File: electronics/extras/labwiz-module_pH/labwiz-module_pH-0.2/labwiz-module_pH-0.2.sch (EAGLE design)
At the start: 14 parts, among them U3 XC6206P182MR, U4 OPA333DBV

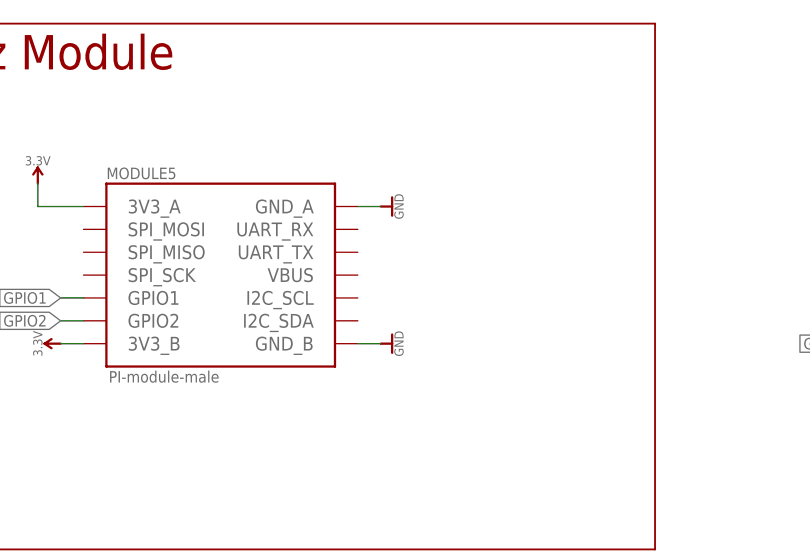
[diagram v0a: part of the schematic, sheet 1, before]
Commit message: Fixed VBUS issues on pH module.
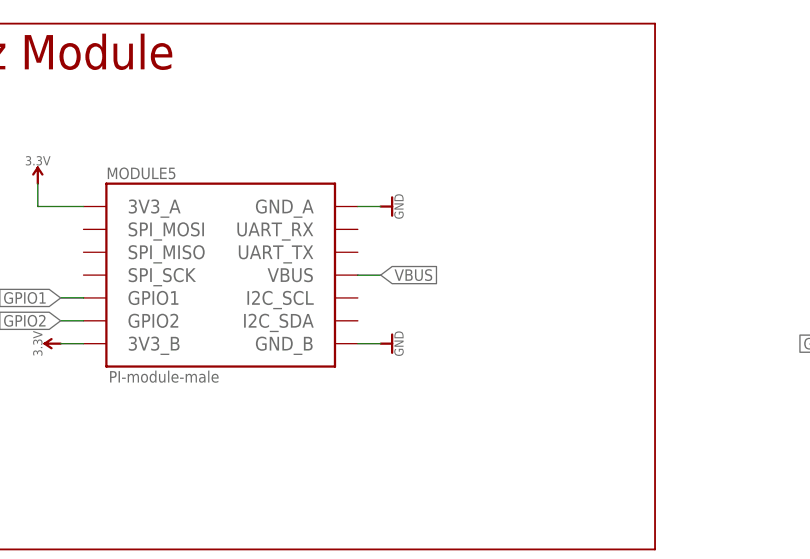
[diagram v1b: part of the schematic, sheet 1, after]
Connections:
- net VBUS: now also MODULE5.VBUS
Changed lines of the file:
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@@
 <grid distance="0.1" unitdist="inch" unit="inch" style="lines" multiple="1" display="no" altdistance="0.01" altunitdist="inch" altunit="inch"/>
 <layers>
-<layer number="1" name="Top" color="4" fill="1" visible="yes" active="no"/>
-<layer number="2" name="Route2" color="1" fill="3" visible="yes" active="no"/>
-<layer number="3" name="Route3" color="4" fill="3" visible="yes" active="no"/>
-<layer number="4" name="Route4" color="1" fill="4" visible="yes" active="no"/>
-<layer number="5" name="Route5" color="4" fill="4" visible="yes" active="no"/>
-<layer number="6" name="Route6" color="1" fill="8" visible="yes" active="no"/>
-<layer number="7" name="Route7" color="4" fill="8" visible="yes" active="no"/>
-<layer number="8" name="Route8" color="1" fill="2" visible="yes" active="no"/>
-<layer number="9" name="Route9" color="4" fill="2" visible="yes" active="no"/>
-<layer number="10" name="Route10" color="1" fill="7" visible="yes" active="no"/>
-<layer number="11" name="Route11" color="4" fill="7" visible="yes" active="no"/>
-<layer number="12" name="Route12" color="1" fill="5" visible="yes" active="no"/>
-<layer number="13" name="Route13" color="4" fill="5" visible="yes" active="no"/>
-<layer number="14" name="Route14" color="1" fill="6" visible="yes" active="no"/>
-<layer number="15" name="Route15" color="4" fill="6" visible="yes" active="no"/>
-<layer number="16" name="Bottom" color="1" fill="1" visible="yes" active="no"/>
-<layer number="17" name="Pads" color="2" fill="1" visible="yes" active="no"/>
-<layer number="18" name="Vias" color="2" fill="1" visible="yes" active="no"/>
-<layer number="19" name="Unrouted" color="6" fill="1" visible="yes" active="no"/>
-<layer number="20" name="Dimension" color="13" fill="1" visible="yes" active="no"/>
-<layer number="21" name="tPlace" color="7" fill="1" visible="yes" active="no"/>
-<layer number="22" name="bPlace" color="14" fill="1" visible="yes" active="no"/>
-<layer number="23" name="tOrigins" color="15" fill="1" visible="yes" active="no"/>
-<layer number="24" name="bOrigins" color="15" fill="1" visible="yes" active="no"/>
-<layer number="25" name="tNames" color="7" fill="1" visible="yes" active="no"/>
-<layer number="26" name="bNames" color="7" fill="1" visible="yes" active="no"/>
-<layer number="27" name="tValues" color="7" fill="1" visible="yes" active="no"/>
-<layer number="28" name="bValues" color="7" fill="1" visible="yes" active="no"/>
+<layer number="1" name="Top" color="4" fill="1" visible="no" active="no"/>
+<layer number="2" name="Route2" color="1" fill="3" visible="no" active="no"/>
+<layer number="3" name="Route3" color="4" fill="3" visible="no" active="no"/>
+<layer number="4" name="Route4" color="1" fill="4" visible="no" active="no"/>
+<layer number="5" name="Route5" color="4" fill="4" visible="no" active="no"/>
+<layer number="6" name="Route6" color="1" fill="8" visible="no" active="no"/>
+<layer number="7" name="Route7" color="4" fill="8" visible="no" active="no"/>
+<layer number="8" name="Route8" color="1" fill="2" visible="no" active="no"/>
+<layer number="9" name="Route9" color="4" fill="2" visible="no" active="no"/>
+<layer number="10" name="Route10" color="1" fill="7" visible="no" active="no"/>
+<layer number="11" name="Route11" color="4" fill="7" visible="no" active="no"/>
+<layer number="12" name="Route12" color="1" fill="5" visible="no" active="no"/>
+<layer number="13" name="Route13" color="4" fill="5" visible="no" active="no"/>
+<layer number="14" name="Route14" color="1" fill="6" visible="no" active="no"/>
+<layer number="15" name="Route15" color="4" fill="6" visible="no" active="no"/>
+<layer number="16" name="Bottom" color="1" fill="1" visible="no" active="no"/>
+<layer number="17" name="Pads" color="2" fill="1" visible="no" active="no"/>
+<layer number="18" name="Vias" color="2" fill="1" visible="no" active="no"/>
+<layer number="19" name="Unrouted" color="6" fill="1" visible="no" active="no"/>
+<layer number="20" name="Dimension" color="13" fill="1" visible="no" active="no"/>
+<layer number="21" name="tPlace" color="7" fill="1" visible="no" active="no"/>
+<layer number="22" name="bPlace" color="14" fill="1" visible="no" active="no"/>
+<layer number="23" name="tOrigins" color="15" fill="1" visible="no" active="no"/>
+<layer number="24" name="bOrigins" color="15" fill="1" visible="no" active="no"/>
+<layer number="25" name="tNames" color="7" fill="1" visible="no" active="no"/>
+<layer number="26" name="bNames" color="7" fill="1" visible="no" active="no"/>
+<layer number="27" name="tValues" color="7" fill="1" visible="no" active="no"/>
+<layer number="28" name="bValues" color="7" fill="1" visible="no" active="no"/>
 <layer number="29" name="tStop" color="7" fill="3" visible="no" active="no"/>
 <layer number="30" name="bStop" color="7" fill="6" visible="no" active="no"/>
@@
 <layer number="35" name="tGlue" color="7" fill="4" visible="no" active="no"/>
 <layer number="36" name="bGlue" color="7" fill="5" visible="no" active="no"/>
-<layer number="37" name="tTest" color="7" fill="1" visible="yes" active="no"/>
-<layer number="38" name="bTest" color="7" fill="1" visible="yes" active="no"/>
+<layer number="37" name="tTest" color="7" fill="1" visible="no" active="no"/>
+<layer number="38" name="bTest" color="7" fill="1" visible="no" active="no"/>
 <layer number="39" name="tKeepout" color="4" fill="11" visible="no" active="no"/>
 <layer number="40" name="bKeepout" color="1" fill="11" visible="no" active="no"/>
@@
 <layer number="44" name="Drills" color="7" fill="1" visible="no" active="no"/>
 <layer number="45" name="Holes" color="7" fill="1" visible="no" active="no"/>
-<layer number="46" name="Milling" color="3" fill="1" visible="yes" active="no"/>
-<layer number="47" name="Measures" color="7" fill="1" visible="yes" active="no"/>
-<layer number="48" name="Document" color="7" fill="1" visible="yes" active="no"/>
-<layer number="49" name="Reference" color="7" fill="1" visible="yes" active="no"/>
-<layer number="50" name="dxf" color="7" fill="1" visible="yes" active="no"/>
-<layer number="51" name="tDocu" color="6" fill="1" visible="yes" active="no"/>
-<layer number="52" name="bDocu" color="7" fill="1" visible="yes" active="no"/>
-<layer number="53" name="tGND_GNDA" color="7" fill="9" visible="yes" active="no"/>
-<layer number="54" name="bGND_GNDA" color="1" fill="9" visible="yes" active="no"/>
-<layer number="56" name="wert" color="7" fill="1" visible="yes" active="no"/>
-<layer number="57" name="tCAD" color="7" fill="1" visible="yes" active="no"/>
-<layer number="59" name="tCarbon" color="7" fill="1" visible="yes" active="no"/>
-<layer number="60" name="bCarbon" color="7" fill="1" visible="yes" active="no"/>
+<layer number="46" name="Milling" color="3" fill="1" visible="no" active="no"/>
+<layer number="47" name="Measures" color="7" fill="1" visible="no" active="no"/>
+<layer number="48" name="Document" color="7" fill="1" visible="no" active="no"/>
+<layer number="49" name="Reference" color="7" fill="1" visible="no" active="no"/>
+<layer number="50" name="dxf" color="7" fill="1" visible="no" active="no"/>
+<layer number="51" name="tDocu" color="6" fill="1" visible="no" active="no"/>
+<layer number="52" name="bDocu" color="7" fill="1" visible="no" active="no"/>
+<layer number="53" name="tGND_GNDA" color="7" fill="9" visible="no" active="no"/>
+<layer number="54" name="bGND_GNDA" color="1" fill="9" visible="no" active="no"/>
+<layer number="56" name="wert" color="7" fill="1" visible="no" active="no"/>
+<layer number="57" name="tCAD" color="7" fill="1" visible="no" active="no"/>
+<layer number="59" name="tCarbon" color="7" fill="1" visible="no" active="no"/>
+<layer number="60" name="bCarbon" color="7" fill="1" visible="no" active="no"/>
 <layer number="90" name="Modules" color="5" fill="1" visible="yes" active="yes"/>
 <layer number="91" name="Nets" color="2" fill="1" visible="yes" active="yes"/>
@@
 <label x="30.48" y="165.1" size="1.27" layer="95" rot="R180" xref="yes"/>
 </segment>
-</net>
+<segment>
+<pinref part="MODULE5" gate="G$1" pin="VBUS"/>
+<wire x1="63.5" y1="226.06" x2="66.04" y2="226.06" width="0.1524" layer="91"/>
+<label x="66.04" y="226.06" size="1.27" layer="95" xref="yes"/>
+</segment>
+</net>

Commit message: Small changes. Not sure what.
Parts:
- C3, C4: value CAPACITOR_FIXED_0603 -> 51pF
- R1, R2: value RESISTOR_FIXED_0603 -> 510k
- R4: value RESISTOR_FIXED_0603 -> 51k
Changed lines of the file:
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@@
 <part name="C8" library="PaxInstruments-RCL" deviceset="CAPACITOR_FIXED" device="_0603" technology="_100NF" value="100nF"/>
 <part name="U3" library="IC" deviceset="XC6206" device="MR" value="XC6206P182MR"/>
-<part name="R1" library="PaxInstruments-RCL" deviceset="RESISTOR_FIXED" device="_0603" value=""/>
+<part name="R1" library="PaxInstruments-RCL" deviceset="RESISTOR_FIXED" device="_0603" value="510k"/>
 <part name="U4" library="IC" deviceset="OPA333" device="DBV"/>
 <part name="C1" library="PaxInstruments-RCL" deviceset="CAPACITOR_FIXED" device="_0603" technology="_100NF" value="100nF"/>
 <part name="GND3" library="PaxInstruments-Aesthetics" deviceset="GND" device="" value="GND"/>
 <part name="GND4" library="PaxInstruments-Aesthetics" deviceset="GND" device="" value="GND"/>
-<part name="R2" library="PaxInstruments-RCL" deviceset="RESISTOR_FIXED" device="_0603" value=""/>
+<part name="R2" library="PaxInstruments-RCL" deviceset="RESISTOR_FIXED" device="_0603" value="510k"/>
 <part name="SUPPLY3" library="PaxInstruments-Aesthetics" deviceset="SYM_VCC" device="" technology="3.3V" value="3.3V"/>
-<part name="C3" library="PaxInstruments-RCL" deviceset="CAPACITOR_FIXED" device="_0603" value=""/>
+<part name="C3" library="PaxInstruments-RCL" deviceset="CAPACITOR_FIXED" device="_0603" value="51pF"/>
 <part name="GND5" library="PaxInstruments-Aesthetics" deviceset="GND" device="" value="GND"/>
-<part name="R4" library="PaxInstruments-RCL" deviceset="RESISTOR_FIXED" device="_0603" value=""/>
-<part name="C4" library="PaxInstruments-RCL" deviceset="CAPACITOR_FIXED" device="_0603" value=""/>
+<part name="R4" library="PaxInstruments-RCL" deviceset="RESISTOR_FIXED" device="_0603" value="51k"/>
+<part name="C4" library="PaxInstruments-RCL" deviceset="CAPACITOR_FIXED" device="_0603" value="51pF"/>
 <part name="GND6" library="PaxInstruments-Aesthetics" deviceset="GND" device="" value="GND"/>
 <part name="J1" library="SparkFun-Connectors" deviceset="M03" device="LOCK_LONGPADS"/>
